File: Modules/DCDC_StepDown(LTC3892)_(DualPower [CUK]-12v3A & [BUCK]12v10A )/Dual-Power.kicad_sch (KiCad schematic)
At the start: 81 parts, among them J1 Conn_02x05_Top_Bottom, J2 Conn_02x05_Top_Bottom, J3 Conn_01x02, Q1 BSC028N06LS3, Q2 BSC028N06LS3, Q3 BSC028N06LS3, Q4 BSC028N06LS3, Q5 BSC028N06LS3, U1 LTC3892EUHPBF, U2 LT1797

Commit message: update readme
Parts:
- L1, L2: value 18uH -> 6.8uH
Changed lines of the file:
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@@
     (in_bom yes) (on_board yes)
     (property "Reference" "L1" (id 0) (at 140.97 194.564 90))
-    (property "Value" "18uH" (id 1) (at 140.97 196.8754 90))
+    (property "Value" "6.8uH" (id 1) (at 140.97 196.8754 90))
     (property "Footprint" "Inductor_SMD:L_Wuerth_HCM-1350" (id 2) (at 140.97 199.39 0)
       (effects (font (size 1.27 1.27)) hide)
@@
     (in_bom yes) (on_board yes)
     (property "Reference" "L2" (id 0) (at 156.21 181.864 90))
-    (property "Value" "18uH" (id 1) (at 156.21 184.1754 90))
+    (property "Value" "6.8uH" (id 1) (at 156.21 184.1754 90))
     (property "Footprint" "Inductor_SMD:L_Wuerth_HCM-1350" (id 2) (at 156.21 186.69 0)
       (effects (font (size 1.27 1.27)) hide)
@@
     )
     (path "/00000000-0000-0000-0000-0000619f13b5"
-      (reference "L1") (unit 1) (value "18uH") (footprint "Inductor_SMD:L_Wuerth_HCM-1350")
+      (reference "L1") (unit 1) (value "6.8uH") (footprint "Inductor_SMD:L_Wuerth_HCM-1350")
     )
     (path "/00000000-0000-0000-0000-00006188029f"
-      (reference "L2") (unit 1) (value "18uH") (footprint "Inductor_SMD:L_Wuerth_HCM-1350")
+      (reference "L2") (unit 1) (value "6.8uH") (footprint "Inductor_SMD:L_Wuerth_HCM-1350")
     )
     (path "/00000000-0000-0000-0000-0000617a9746"

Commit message: update Dual-power
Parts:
- R7: value 7K -> 10K
- R8: value 10K -> 20K
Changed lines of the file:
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@@
     (in_bom yes) (on_board yes)
     (property "Reference" "R7" (id 0) (at 252.73 105.41 90))
-    (property "Value" "7K" (id 1) (at 248.92 104.14 90))
+    (property "Value" "10K" (id 1) (at 248.92 104.14 90))
     (property "Footprint" "Resistor_SMD:R_0402_1005Metric" (id 2) (at 252.73 107.188 90)
       (effects (font (size 1.27 1.27)) hide)
@@
     (in_bom yes) (on_board yes)
     (property "Reference" "R8" (id 0) (at 252.73 109.22 90))
-    (property "Value" "10K" (id 1) (at 248.92 107.95 90))
+    (property "Value" "20K" (id 1) (at 248.92 107.95 90))
     (property "Footprint" "Resistor_SMD:R_0402_1005Metric" (id 2) (at 252.73 110.998 90)
       (effects (font (size 1.27 1.27)) hide)
@@
     )
     (path "/00000000-0000-0000-0000-000061576094"
-      (reference "R7") (unit 1) (value "7K") (footprint "Resistor_SMD:R_0402_1005Metric")
+      (reference "R7") (unit 1) (value "10K") (footprint "Resistor_SMD:R_0402_1005Metric")
     )
     (path "/00000000-0000-0000-0000-00006157608e"
-      (reference "R8") (unit 1) (value "10K") (footprint "Resistor_SMD:R_0402_1005Metric")
+      (reference "R8") (unit 1) (value "20K") (footprint "Resistor_SMD:R_0402_1005Metric")
     )
     (path "/00000000-0000-0000-0000-0000617d541c"

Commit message: update Dual-power
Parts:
- C11: value 1nF -> 6.8nF
- C12: value 100pF -> 47pF
- C21, C25: value 1nF -> 220pF
- C5: value 10nF -> 6.8nF
- C6: value 330pF -> 47pF
- R3: value 7.5K -> 10K
- R4: value 34.8K -> 10K
- R5: value 100K -> 31.6K
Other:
- note added: "Q1\Q2\Q5 BSC028N OR BSC026N Q3\Q4 BSC100N OR BSC117N"
- note removed: "Q1\Q2\Q5 BSC28N Q3\Q4 BSC100N"
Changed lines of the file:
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@@
     (stroke (width 0) (type default) (color 0 0 0 0))
   )
-  (polyline (pts (xy 265.43 196.85) (xy 298.45 196.85))
+  (polyline (pts (xy 265.43 196.85) (xy 300.99 196.85))
     (stroke (width 0) (type default) (color 0 0 0 0))
   )
@@
     (stroke (width 0) (type default) (color 0 0 0 0))
   )
-  (polyline (pts (xy 298.45 196.85) (xy 298.45 210.82))
+  (polyline (pts (xy 300.99 196.85) (xy 300.99 210.82))
     (stroke (width 0) (type default) (color 0 0 0 0))
   )
-  (polyline (pts (xy 298.45 210.82) (xy 265.43 210.82))
+  (polyline (pts (xy 300.99 210.82) (xy 265.43 210.82))
     (stroke (width 0) (type default) (color 0 0 0 0))
   )
@@
     (effects (font (size 1.27 1.27)) (justify left bottom))
   )
-  (text "Q1\\Q2\\Q5 BSC28N\nQ3\\Q4 BSC100N" (at 266.7 208.28 0)
+  (text "Q1\\Q2\\Q5 BSC028N OR BSC026N\nQ3\\Q4 BSC100N OR BSC117N"
+    (at 266.7 208.28 0)
     (effects (font (size 1.27 1.27)) (justify left bottom))
   )
@@
     (in_bom yes) (on_board yes)
     (property "Reference" "R3" (id 0) (at 181.61 143.51 90))
-    (property "Value" "7.5K" (id 1) (at 181.61 146.05 90))
+    (property "Value" "10K" (id 1) (at 181.61 146.05 90))
     (property "Footprint" "Resistor_SMD:R_0402_1005Metric" (id 2) (at 181.61 141.732 90)
       (effects (font (size 1.27 1.27)) hide)
@@
     (in_bom yes) (on_board yes)
     (property "Reference" "R4" (id 0) (at 236.22 143.51 90))
-    (property "Value" "34.8K" (id 1) (at 236.22 146.05 90))
+    (property "Value" "10K" (id 1) (at 236.22 146.05 90))
     (property "Footprint" "Resistor_SMD:R_0402_1005Metric" (id 2) (at 236.22 141.732 90)
       (effects (font (size 1.27 1.27)) hide)
@@
     (in_bom yes) (on_board yes)
     (property "Reference" "R5" (id 0) (at 238.76 91.44 90))
-    (property "Value" "100K" (id 1) (at 233.68 90.17 90))
+    (property "Value" "31.6K" (id 1) (at 233.68 90.17 90))
     (property "Footprint" "Resistor_SMD:R_0402_1005Metric" (id 2) (at 238.76 89.662 90)
       (effects (font (size 1.27 1.27)) hide)
@@
       (effects (font (size 1.27 1.27)) (justify left))
     )
-    (property "Value" "10nF" (id 1) (at 176.53 142.24 90)
+    (property "Value" "6.8nF" (id 1) (at 176.53 142.24 90)
       (effects (font (size 1.27 1.27)) (justify left))
     )
@@
       (effects (font (size 1.27 1.27)) (justify left))
     )
-    (property "Value" "330pF" (id 1) (at 177.8 148.59 90)
+    (property "Value" "47pF" (id 1) (at 177.8 148.59 90)
       (effects (font (size 1.27 1.27)) (justify left))
     )
@@
       (effects (font (size 1.27 1.27)) (justify left))
     )
-    (property "Value" "1nF" (id 1) (at 173.99 166.37 0)
+    (property "Value" "220pF" (id 1) (at 173.99 166.37 0)
       (effects (font (size 1.27 1.27)) (justify left))
     )
@@
       (effects (font (size 1.27 1.27)) (justify left))
     )
-    (property "Value" "1nF" (id 1) (at 247.65 142.24 90)
+    (property "Value" "6.8nF" (id 1) (at 247.65 142.24 90)
       (effects (font (size 1.27 1.27)) (justify left))
     )
@@
       (effects (font (size 1.27 1.27)) (justify left))
     )
-    (property "Value" "100pF" (id 1) (at 247.65 148.59 90)
+    (property "Value" "47pF" (id 1) (at 247.65 148.59 90)
       (effects (font (size 1.27 1.27)) (justify left))
     )
@@
       (effects (font (size 1.27 1.27)) (justify left))
     )
-    (property "Value" "1nF" (id 1) (at 292.1 175.26 90)
+    (property "Value" "220pF" (id 1) (at 292.1 175.26 90)
       (effects (font (size 1.27 1.27)) (justify left))
     )
@@
     )
     (path "/00000000-0000-0000-0000-0000616da52e"
-      (reference "C5") (unit 1) (value "10nF") (footprint "Capacitor_SMD:C_0402_1005Metric")
+      (reference "C5") (unit 1) (value "6.8nF") (footprint "Capacitor_SMD:C_0402_1005Metric")
     )
     (path "/00000000-0000-0000-0000-0000616e74b1"
-      (reference "C6") (unit 1) (value "330pF") (footprint "Capacitor_SMD:C_0402_1005Metric")
+      (reference "C6") (unit 1) (value "47pF") (footprint "Capacitor_SMD:C_0402_1005Metric")
     )
     (path "/00000000-0000-0000-0000-0000616365b8"
@@
     )
     (path "/00000000-0000-0000-0000-0000616d1f0d"
-      (reference "C11") (unit 1) (value "1nF") (footprint "Capacitor_SMD:C_0402_1005Metric")
+      (reference "C11") (unit 1) (value "6.8nF") (footprint "Capacitor_SMD:C_0402_1005Metric")
     )
     (path "/00000000-0000-0000-0000-0000616e205c"
-      (reference "C12") (unit 1) (value "100pF") (footprint "Capacitor_SMD:C_0402_1005Metric")
+      (reference "C12") (unit 1) (value "47pF") (footprint "Capacitor_SMD:C_0402_1005Metric")
     )
     (path "/00000000-0000-0000-0000-00006157968d"
@@
     )
     (path "/00000000-0000-0000-0000-00006191d4b8"
-      (reference "C21") (unit 1) (value "1nF") (footprint "Capacitor_SMD:C_0402_1005Metric")
+      (reference "C21") (unit 1) (value "220pF") (footprint "Capacitor_SMD:C_0402_1005Metric")
     )
     (path "/00000000-0000-0000-0000-000061aca1e0"
@@
     )
     (path "/00000000-0000-0000-0000-0000617eb53a"
-      (reference "C25") (unit 1) (value "1nF") (footprint "Capacitor_SMD:C_0402_1005Metric")
+      (reference "C25") (unit 1) (value "220pF") (footprint "Capacitor_SMD:C_0402_1005Metric")
     )
     (path "/00000000-0000-0000-0000-000061860a7f"
@@
     )
     (path "/00000000-0000-0000-0000-0000616d7075"
-      (reference "R3") (unit 1) (value "7.5K") (footprint "Resistor_SMD:R_0402_1005Metric")
+      (reference "R3") (unit 1) (value "10K") (footprint "Resistor_SMD:R_0402_1005Metric")
     )
     (path "/00000000-0000-0000-0000-0000616d8871"
-      (reference "R4") (unit 1) (value "34.8K") (footprint "Resistor_SMD:R_0402_1005Metric")
+      (reference "R4") (unit 1) (value "10K") (footprint "Resistor_SMD:R_0402_1005Metric")
     )
     (path "/00000000-0000-0000-0000-000061565c83"
-      (reference "R5") (unit 1) (value "100K") (footprint "Resistor_SMD:R_0402_1005Metric")
+      (reference "R5") (unit 1) (value "31.6K") (footprint "Resistor_SMD:R_0402_1005Metric")
     )
     (path "/00000000-0000-0000-0000-00006156e3f7"

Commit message: update dual_power
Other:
- note added: "For -16V R10 = 127.75K R11 = 4.91K"
- note added: "For 16V R16 = 190K R15 = 10K"
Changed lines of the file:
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@@
+    (stroke (width 0) (type default) (color 0 0 0 0))
+  )
+  (polyline (pts (xy 101.6 151.13) (xy 101.6 161.29))
+    (stroke (width 0) (type default) (color 0 0 0 0))
+  )
+  (polyline (pts (xy 101.6 161.29) (xy 119.38 161.29))
     (stroke (width 0) (type default) (color 0 0 0 0))
   )
@@
     (stroke (width 0) (type default) (color 0 0 0 0))
   )
+  (polyline (pts (xy 119.38 151.13) (xy 101.6 151.13))
+    (stroke (width 0) (type default) (color 0 0 0 0))
+  )
+  (polyline (pts (xy 119.38 161.29) (xy 119.38 151.13))
+    (stroke (width 0) (type default) (color 0 0 0 0))
+  )
   (polyline (pts (xy 119.38 162.56) (xy 101.6 162.56))
     (stroke (width 0) (type default) (color 0 0 0 0))
@@
     (stroke (width 0) (type default) (color 0 0 0 0))
   )
+  (polyline (pts (xy 316.23 166.37) (xy 316.23 177.8))
+    (stroke (width 0) (type default) (color 0 0 0 0))
+  )
+  (polyline (pts (xy 316.23 177.8) (xy 331.47 177.8))
+    (stroke (width 0) (type default) (color 0 0 0 0))
+  )
   (polyline (pts (xy 321.31 201.93) (xy 331.47 201.93))
     (stroke (width 0) (type default) (color 0 0 0 0))
@@
     (stroke (width 0) (type default) (color 0 0 0 0))
   )
+  (polyline (pts (xy 331.47 166.37) (xy 316.23 166.37))
+    (stroke (width 0) (type default) (color 0 0 0 0))
+  )
+  (polyline (pts (xy 331.47 177.8) (xy 331.47 166.37))
+    (stroke (width 0) (type default) (color 0 0 0 0))
+  )
   (polyline (pts (xy 331.47 201.93) (xy 331.47 205.74))
     (stroke (width 0) (type default) (color 0 0 0 0))
@@
   (polyline (pts (xy 335.28 67.31) (xy 325.12 67.31))
     (stroke (width 0) (type default) (color 0 0 0 0))
+  )
+  (text "For -16V\n\nR10 = 127.75K\nR11 = 4.91K" (at 102.87 160.02 0)
+    (effects (font (size 1.27 1.27)) (justify left bottom))
   )
   (text "For -18V\n\nR10 = 114.75K\nR11 = 4.87K" (at 102.87 171.45 0)
@@
     (effects (font (size 1.27 1.27)) (justify left bottom))
   )
+  (text "For 16V\n\nR16 = 190K\nR15 = 10K" (at 317.5 176.53 0)
+    (effects (font (size 1.27 1.27)) (justify left bottom))
+  )

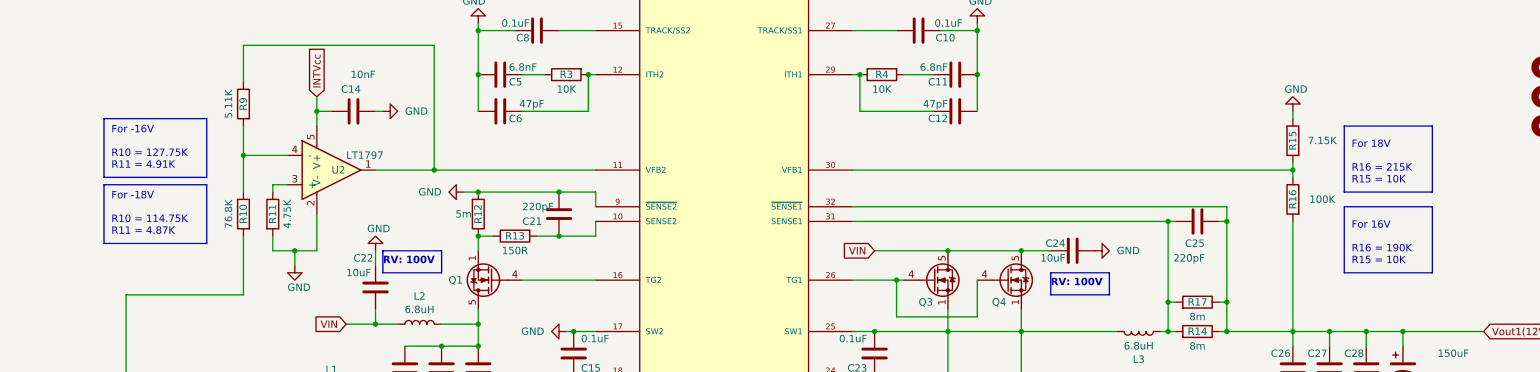
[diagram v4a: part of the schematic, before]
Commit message: update Dual-Power design parameter
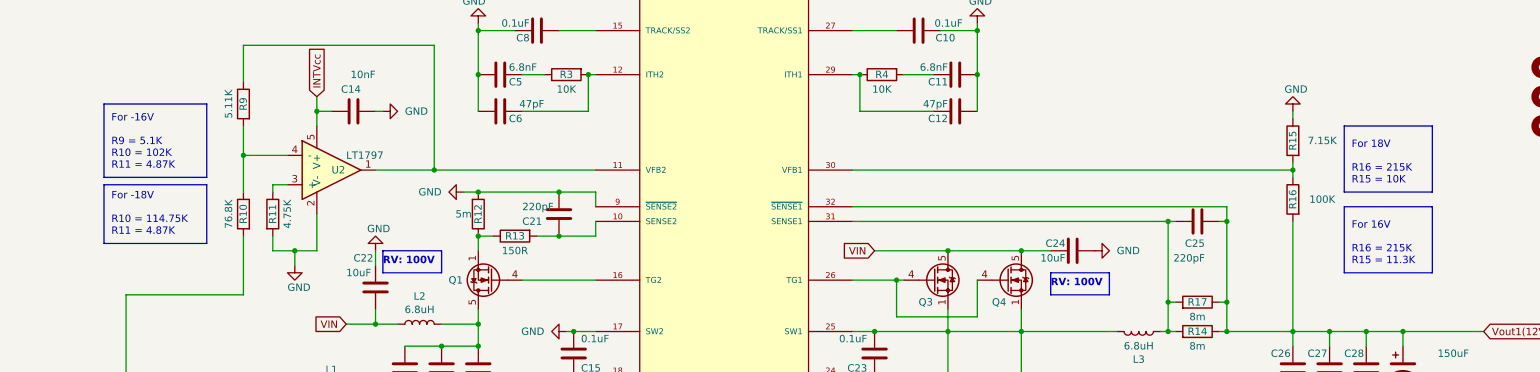
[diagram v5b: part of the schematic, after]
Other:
- note added: "For -16V R9 = 5.1K R10 = 102K R11 = 4.87K"
- note added: "For 16V R16 = 215K R15 = 11.3K"
- note removed: "For -16V R10 = 127.75K R11 = 4.91K"
- note removed: "For 16V R16 = 190K R15 = 10K"
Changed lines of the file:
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@@
     (stroke (width 0) (type default) (color 0 0 0 0))
   )
-  (polyline (pts (xy 101.6 151.13) (xy 101.6 161.29))
+  (polyline (pts (xy 101.6 148.59) (xy 101.6 161.29))
     (stroke (width 0) (type default) (color 0 0 0 0))
   )
@@
     (stroke (width 0) (type default) (color 0 0 0 0))
   )
-  (polyline (pts (xy 119.38 151.13) (xy 101.6 151.13))
-    (stroke (width 0) (type default) (color 0 0 0 0))
-  )
-  (polyline (pts (xy 119.38 161.29) (xy 119.38 151.13))
+  (polyline (pts (xy 119.38 148.59) (xy 101.6 148.59))
+    (stroke (width 0) (type default) (color 0 0 0 0))
+  )
+  (polyline (pts (xy 119.38 161.29) (xy 119.38 148.59))
     (stroke (width 0) (type default) (color 0 0 0 0))
   )
@@
     (stroke (width 0) (type default) (color 0 0 0 0))
   )
-  (text "For -16V\n\nR10 = 127.75K\nR11 = 4.91K" (at 102.87 160.02 0)
+  (text "For -16V\n\nR9 = 5.1K\nR10 = 102K\nR11 = 4.87K" (at 102.87 160.02 0)
     (effects (font (size 1.27 1.27)) (justify left bottom))
   )
@@
     (effects (font (size 1.27 1.27)) (justify left bottom))
   )
-  (text "For 16V\n\nR16 = 190K\nR15 = 10K" (at 317.5 176.53 0)
-    (effects (font (size 1.27 1.27)) (justify left bottom))
-  )
+  (text "For 16V\n\nR16 = 215K\nR15 = 11.3K" (at 317.5 176.53 0)
+    (effects (font (size 1.27 1.27)) (justify left bottom))
+  )
